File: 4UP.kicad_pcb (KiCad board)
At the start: 4 copper layers, 19 x 108 mm, 35 parts, among them CON1 BARREL_JACK, J1 Conn_01x02_Male, J2 Conn_01x02_Male, J3 Conn_01x02_Male, P1 CONN_02X08, P2 CONN_02X08, SW1 SW_SPST, U1 VX078012-1000, U2 VX078012-1000, U3 VX078-500

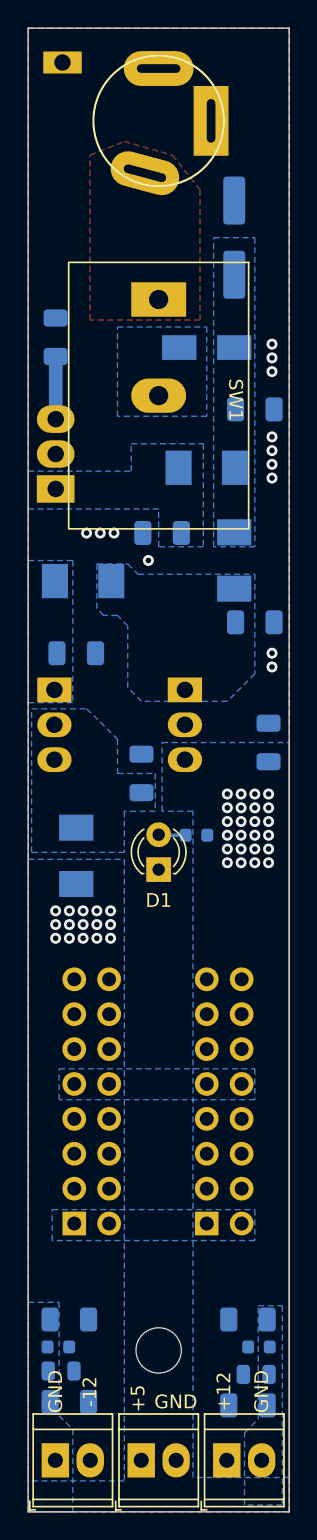
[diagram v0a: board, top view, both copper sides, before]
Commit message: fixed interference between bulk caps and VXO PSUs
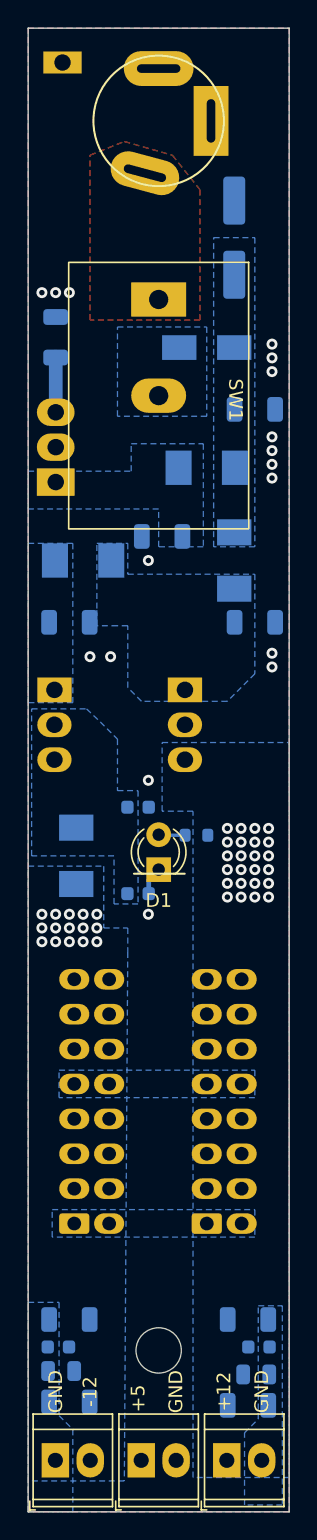
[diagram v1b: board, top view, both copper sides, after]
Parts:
- C12, C13: value 22µ -> 10µ; footprint Capacitor_SMD:C_1206_3216Metric -> Capacitor_SMD:C_0603_1608Metric
- moved C12 14.5 mm to (39.5, 103.2), turned to 180 degrees
- moved C13 2.47 mm to (39.5, 97.0), turned to 180 degrees
- moved C11 2.30 mm to (34.5, 83.5)
- moved L3 1.50 mm to (35.5, 79.0)
- moved U3 0.50 mm to (38.6, 70.8)
- moved C9 0.25 mm to (41.2, 77.2)
- moved REF** 0.25 mm to (41.0, 136.5)
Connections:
- C12 pad 1: +12V -> GND
- C12 pad 2: GND -> Net-(C13-Pad2)
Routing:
- net GND: track 0.73 -> 37.6 mm, vias 13 -> 17
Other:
- board text added: "04/2024"
- board text added: "4UP r1.1"
- board text removed: "10/2022"
- board text removed: "4UP r1.0"

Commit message: ready to order
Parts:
- moved C11 1.52 mm to (36.0, 83.8)
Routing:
- net GND: track 37.6 -> 46.3 mm, vias 17 -> 22
